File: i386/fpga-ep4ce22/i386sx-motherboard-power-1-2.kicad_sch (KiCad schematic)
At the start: 8 parts, among them U8 TPS54620RGYR 12->3V3

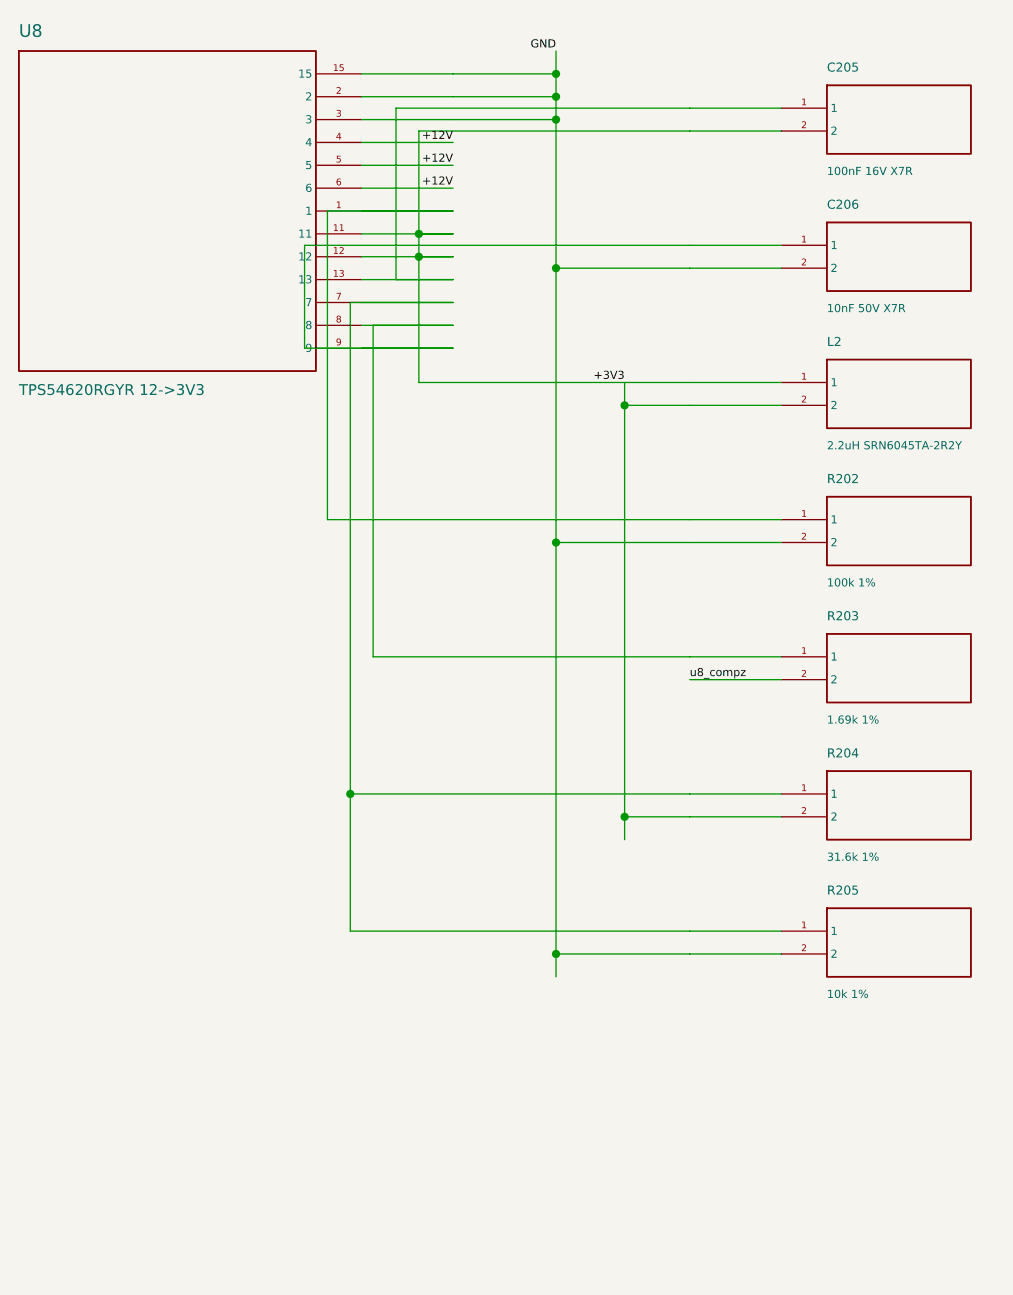
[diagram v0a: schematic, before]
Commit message: Publish the motherboards' KiCad files
From socket3@c0f6464 socket7@9205469 socket370@524f5b1 i386@bea926c
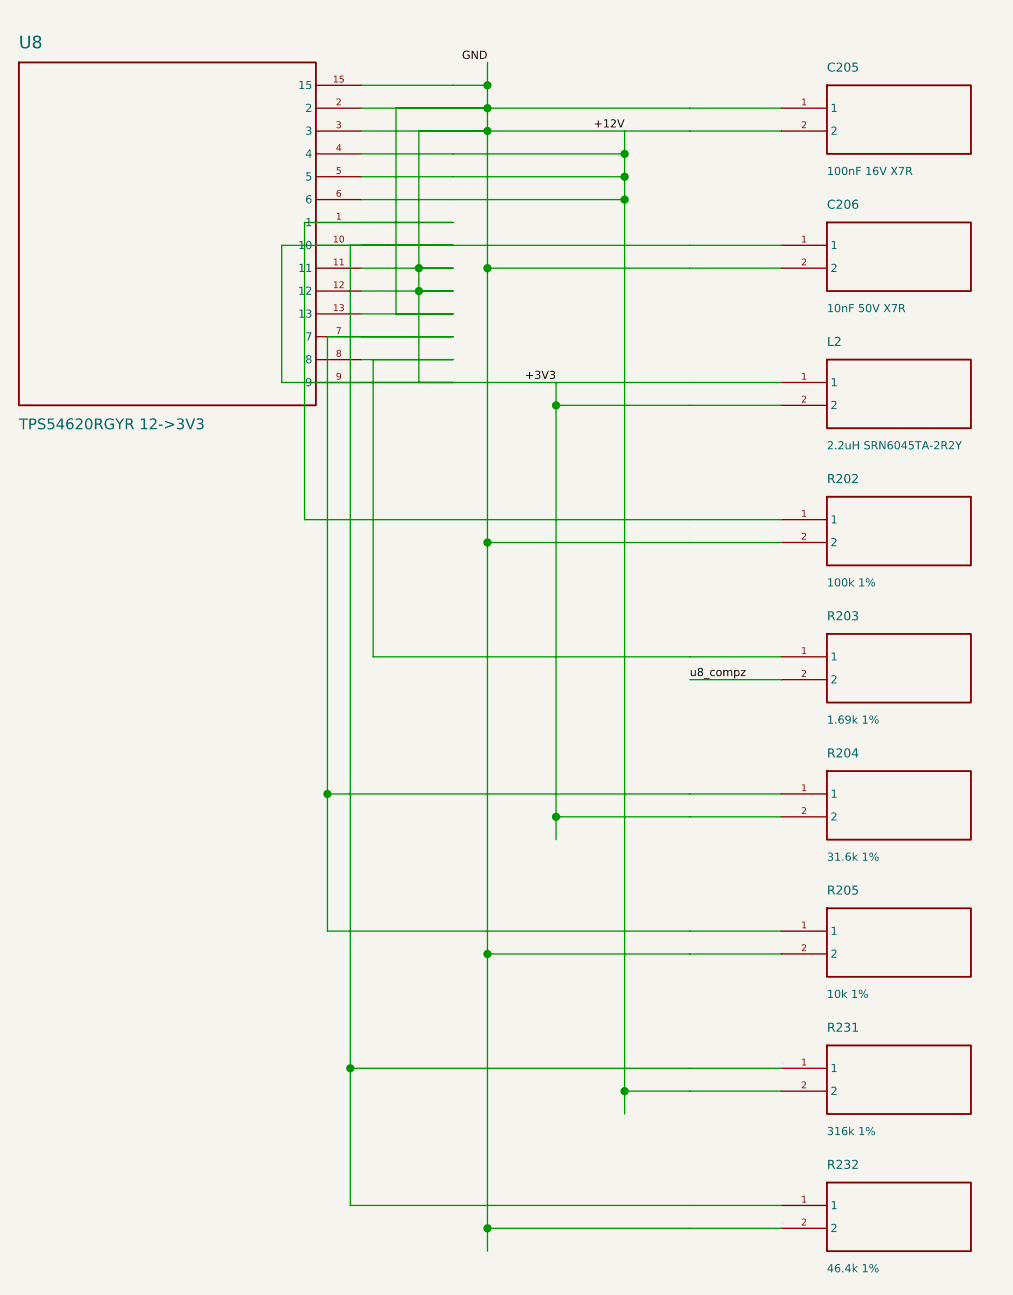
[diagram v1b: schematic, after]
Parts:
- removed U8: TPS54620RGYR 12->3V3, symbol gen:S0_13
- added R231: 316k 1%, symbol gen:S2_0s
- added R232: 46.4k 1%, symbol gen:S2_0s
- added U8: TPS54620RGYR 12->3V3, symbol gen:S0_14
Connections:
- net +3V3 is gone; now on net +12V: C205.2, L2.1, L2.2, R204.2
- net GND is gone; now on net +12V: C206.2, R202.2, R205.2
- net +12V: now also C205.1, C206.1, R231.1, R231.2, R232.1, R232.2, U8.10, U8.11, U8.12, U8.13, U8.15, U8.2, U8.3, U8.4, U8.5, U8.6, U8.9
- net at R202.1: now also U8.1
- net at R204.1, R205.1: now also U8.7
- net at R203.1: now also U8.8
